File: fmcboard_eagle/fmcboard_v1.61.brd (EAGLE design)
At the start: 147 x 74 mm, 208 parts, among them IC1 OPA699ID, IC10 LM358, IC11 7805TV, IC12 SN74AUC2G66DCTR, IC13 SN74AUC2G66DCTR, IC14 SN74AUC2G66DCTR, IC15 SN74AUC2G66DCTR, IC16 DAC7578SPWR, IC17 SN74AUC2G66DCTR, IC18 SN74AUC2G66DCTR, IC19 SN74AUC2G66DCTR, IC2 DAC7578SPWR, IC20 SN74AUC2G66DCTR, IC21 74AUP2GU04GW, IC22 74AUP2GU04GW, IC23 74AUP2GU04GW, IC24 74AUP2GU04GW, IC25 LM358, IC26 AMS1117-1.8, IC3 LTC6229IMS8E#TRPBF, IC4 LTC6229IMS8E#TRPBF, IC5 LTC6229IMS8E#TRPBF, IC6 OPA699ID, IC7 OPA699ID, IC8 LM358, IC9 LM358, J1 8pin, J10 8pin, J11 8pin, J12 4p-2.54, J2 ASP-134604-01, J3 4p-2.54, J4 4p-2.54, J5 8pin, J6 4p-2.54, J7 4p-2.54, J8 4p-2.54, J9 8pin, U1 TXS0108EPWR, U2 STMICROELECTRONICS_L7905ACVST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

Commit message: routed 1.61
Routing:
- net GND: track 0.00 -> 449.9 mm, vias 0 -> 43
- net VS+: track 0.00 -> 330.0 mm, vias 0 -> 6
- net VS-: track 0.00 -> 305.3 mm, vias 0 -> 5
- net 1V8: track 0.00 -> 229.1 mm, vias 0 -> 10
- net SCLIN: track 0.00 -> 186.5 mm, vias 0 -> 2
- net SDAIN: track 0.00 -> 160.5 mm, vias 0 -> 4
- net H34: track 0.00 -> 156.1 mm, vias 0 -> 3
- net OPOUT1_H10: track 0.00 -> 151.4 mm, vias 0 -> 9
- net 1V8-: track 0.00 -> 144.2 mm, vias 0 -> 7
- net OPOUT2_H11: track 0.00 -> 140.5 mm, vias 0 -> 3
- net AR_SDAIN2: track 0.00 -> 136.9 mm, vias 0 -> 4
- net AR_SCLIN2: track 0.00 -> 133.5 mm, vias 0 -> 3
- net G37: track 0.00 -> 110.3 mm, vias 0 -> 2
- net G36: track 0.00 -> 109.7 mm, vias 0 -> 2
- net C10: track 0.00 -> 108.3 mm, vias 0 -> 4
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
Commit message: minor
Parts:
- moved C20 2.00 mm to (83.0, 9.00)
- moved R77 2.00 mm to (83.0, 11.0)
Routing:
- net GND: track 449.9 -> 451.6 mm
- net N$31: track 36.8 -> 35.9 mm, vias 2 -> 4
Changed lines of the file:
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@@
 <drawing>
 <settings>
-<setting alwaysvectorfont="no"/>
+<setting alwaysvectorfont="yes"/>
 <setting verticaltext="up"/>
 </settings>
@@
 <wire x1="38" y1="73" x2="38" y2="1" width="0.1524" layer="21"/>
 <text x="95.4" y="29.5" size="0.8128" layer="21">GNDs</text>
-<wire x1="39" y1="64" x2="139" y2="64" width="0.1524" layer="21"/>
+<wire x1="68" y1="64" x2="139" y2="64" width="0.1524" layer="21"/>
 <wire x1="127" y1="1" x2="127" y2="63" width="0.1524" layer="21"/>
-<wire x1="67" y1="63" x2="67" y2="1" width="0.1524" layer="21"/>
+<wire x1="67" y1="73" x2="67" y2="1" width="0.1524" layer="21"/>
 <wire x1="86" y1="63" x2="86" y2="1" width="0.1524" layer="21"/>
 <wire x1="109" y1="63" x2="109" y2="30" width="0.1524" layer="21"/>
@@
 <attribute name="SPICEPREFIX" value="R" x="71" y="9" size="1.778" layer="27" rot="R180" display="off"/>
 </element>
-<element name="R77" library="rcl" library_urn="urn:adsk.eagle:library:334" package="R0805" package3d_urn="urn:adsk.eagle:package:23553/2" value="100" x="83" y="9" smashed="yes">
-<attribute name="POPULARITY" value="85" x="83" y="9" size="1.778" layer="27" display="off"/>
-<attribute name="SPICEPREFIX" value="R" x="83" y="9" size="1.778" layer="27" display="off"/>
+<element name="R77" library="rcl" library_urn="urn:adsk.eagle:library:334" package="R0805" package3d_urn="urn:adsk.eagle:package:23553/2" value="100" x="83" y="11" smashed="yes">
+<attribute name="POPULARITY" value="85" x="83" y="11" size="1.778" layer="27" display="off"/>
+<attribute name="SPICEPREFIX" value="R" x="83" y="11" size="1.778" layer="27" display="off"/>
 </element>
 <element name="C17" library="SparkFun-Passives" package="0805" value="1uF" x="71" y="24" smashed="yes"/>
 <element name="C18" library="SparkFun-Passives" package="0805" value="1uF" x="83" y="22" smashed="yes" rot="R180"/>
 <element name="C19" library="SparkFun-Passives" package="0805" value="1uF" x="71" y="11" smashed="yes"/>
-<element name="C20" library="SparkFun-Passives" package="0805" value="1uF" x="83" y="11" smashed="yes" rot="R180"/>
+<element name="C20" library="SparkFun-Passives" package="0805" value="1uF" x="83" y="9" smashed="yes" rot="R180"/>
 <element name="J11" library="SparkFun-Connectors" library_urn="urn:adsk.eagle:library:513" package="1X08" package3d_urn="urn:adsk.eagle:package:38138/1" value="8pin" x="88.2" y="31.9" smashed="yes">
 <attribute name="PROD_ID" value="CONN-08438" x="88.2" y="31.9" size="1.778" layer="27" display="off"/>
@@
 <wire x1="64" y1="30.125" x2="64" y2="29" width="0.3048" layer="1"/>
 <wire x1="64" y1="29" x2="63.9" y2="29" width="0.3048" layer="1"/>
-<wire x1="83.875" y1="12.125" x2="83.875" y2="11" width="0.3048" layer="1"/>
-<wire x1="83.875" y1="11" x2="83.9" y2="11" width="0.3048" layer="1"/>
+<wire x1="82.875" y1="7.125" x2="82.875" y2="9" width="0.3048" layer="1"/>
+<wire x1="82.875" y1="9" x2="83.9" y2="9" width="0.3048" layer="1"/>
 <wire x1="78.125" y1="21.125" x2="78.125" y2="20" width="0.3048" layer="1"/>
 <wire x1="78.125" y1="20" x2="78.1" y2="20" width="0.3048" layer="1"/>
@@
 <wire x1="114.25" y1="23" x2="113" y2="23" width="0.3048" layer="1"/>
 <wire x1="113" y1="23" x2="112.938" y2="22.975" width="0.3048" layer="1"/>
-<wire x1="57.125" y1="8.25" x2="57.125" y2="7" width="0.3048" layer="1"/>
-<wire x1="57.125" y1="7" x2="57.05" y2="7" width="0.3048" layer="1"/>
 <wire x1="57.125" y1="8.25" x2="57.279396875" y2="8.25" width="0.3048" layer="2"/>
 <wire x1="88.125" y1="24.25" x2="88.125" y2="23" width="0.3048" layer="1"/>
@@
 <via x="55.875" y="33.125" extent="1-16" drill="0.3048"/>
 <via x="64" y="30.125" extent="1-16" drill="0.3048"/>
-<via x="83.875" y="12.125" extent="1-16" drill="0.3048"/>
+<via x="82.875" y="7.125" extent="1-16" drill="0.3048"/>
 <via x="78.125" y="21.125" extent="1-16" drill="0.3048"/>
 <via x="56.125" y="47" extent="1-16" drill="0.3048"/>
@@
 <wire x1="13.175" y1="45.255" x2="22.205" y2="45.255" width="0.3048" layer="16"/>
 <wire x1="22.205" y1="45.255" x2="23" y2="46.05" width="0.3048" layer="16"/>
+<wire x1="57.125" y1="8.25" x2="57.125" y2="7.075" width="0.3048" layer="1"/>
+<wire x1="57.125" y1="7.075" x2="57.05" y2="7" width="0.3048" layer="1"/>
 </signal>
 <signal name="IO1">
@@
 <wire x1="80.625" y1="8.25" x2="79" y2="8.25" width="0.3048" layer="15"/>
 <wire x1="81.25" y1="8.25" x2="80.625" y2="8.25" width="0.3048" layer="1"/>
-<wire x1="82" y1="9" x2="81.25" y2="8.25" width="0.3048" layer="1"/>
+<wire x1="82.05" y1="9.05" x2="81.25" y2="8.25" width="0.3048" layer="1"/>
 <wire x1="79" y1="9" x2="78.95" y2="9.025" width="0.3048" layer="1"/>
-<wire x1="82" y1="9" x2="82.05" y2="9" width="0.3048" layer="1"/>
-<wire x1="82.125" y1="9.125" x2="82.125" y2="11" width="0.3048" layer="1"/>
-<wire x1="82.125" y1="11" x2="82.1" y2="11" width="0.3048" layer="1"/>
-<wire x1="82.125" y1="9.125" x2="82.05" y2="9" width="0.3048" layer="1"/>
 <via x="79" y="8.25" extent="1-16" drill="0.3048"/>
 <via x="80.625" y="8.25" extent="1-16" drill="0.3048"/>
+<wire x1="82.1" y1="9" x2="82.05" y2="9.05" width="0.3048" layer="1"/>
+<wire x1="82.05" y1="9.05" x2="82.05" y2="11" width="0.3048" layer="1"/>
 </signal>
 <signal name="N$16">
@@
 <wire x1="54.875" y1="19.75" x2="54.8" y2="19.635" width="0.3048" layer="1"/>
 <wire x1="57" y1="21" x2="57.05" y2="21" width="0.3048" layer="1"/>
-<wire x1="83.875" y1="9.25" x2="83.875" y2="9" width="0.3048" layer="1"/>
-<wire x1="83" y1="10.125" x2="83.875" y2="9.25" width="0.3048" layer="1"/>
-<wire x1="79" y1="10.125" x2="83" y2="10.125" width="0.3048" layer="15"/>
-<wire x1="70.75" y1="18.375" x2="79" y2="10.125" width="0.3048" layer="15"/>
 <wire x1="70.25" y1="18.375" x2="70.75" y2="18.375" width="0.3048" layer="1"/>
 <wire x1="65.25" y1="23.375" x2="70.25" y2="18.375" width="0.3048" layer="1"/>
 <wire x1="59.375" y1="23.375" x2="65.25" y2="23.375" width="0.3048" layer="1"/>
 <wire x1="57.125" y1="21.125" x2="59.375" y2="23.375" width="0.3048" layer="1"/>
-<wire x1="83.875" y1="9" x2="83.95" y2="9" width="0.3048" layer="1"/>
 <wire x1="57.125" y1="21.125" x2="57.05" y2="21" width="0.3048" layer="1"/>
-<via x="83" y="10.125" extent="1-16" drill="0.3048"/>
 <via x="70.75" y="18.375" extent="1-16" drill="0.3048"/>
+<wire x1="83.95" y1="11" x2="81.95" y2="13" width="0.3048" layer="1"/>
+<wire x1="81.95" y1="13" x2="81" y2="13" width="0.3048" layer="1"/>
+<via x="81" y="13" extent="1-16" drill="0.35"/>
+<wire x1="81" y1="13" x2="79" y2="13" width="0.3048" layer="15"/>
+<via x="79" y="13" extent="1-16" drill="0.35"/>
+<wire x1="79" y1="13" x2="76" y2="13" width="0.3048" layer="1"/>
+<wire x1="76" y1="13" x2="75" y2="14" width="0.3048" layer="1"/>
+<via x="75" y="14" extent="1-16" drill="0.35"/>
+<wire x1="75" y1="14" x2="70.75" y2="18.25" width="0.3048" layer="15"/>
+<wire x1="70.75" y1="18.25" x2="70.75" y2="18.375" width="0.3048" layer="15"/>
 </signal>
 <signal name="N$32">

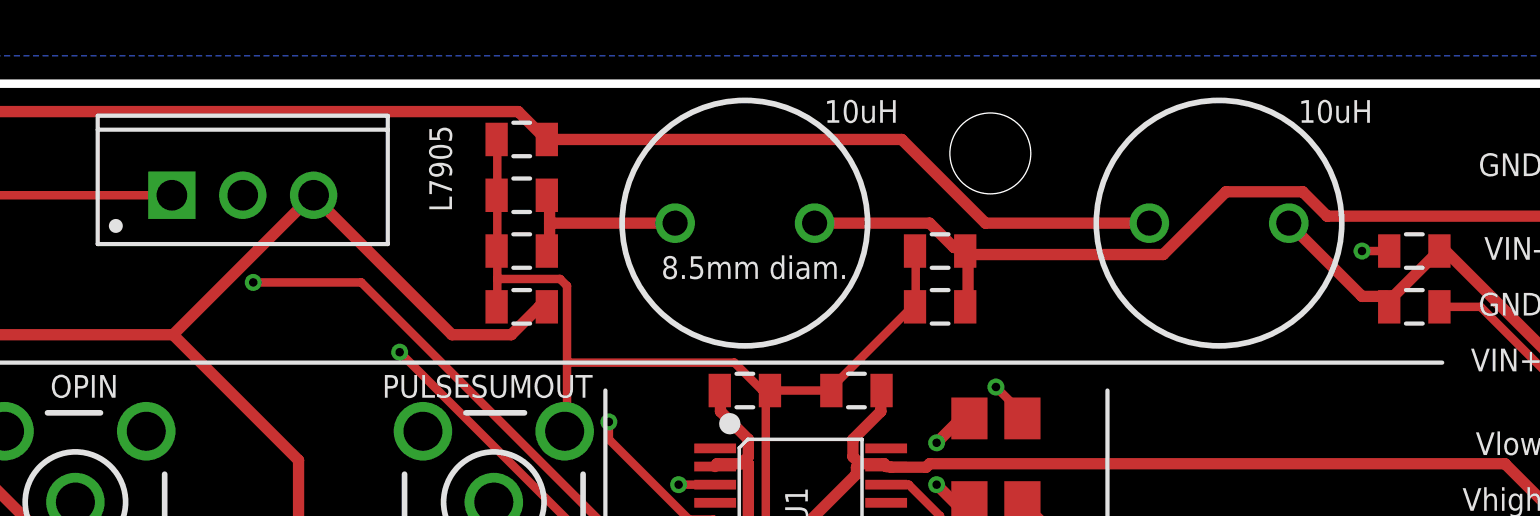
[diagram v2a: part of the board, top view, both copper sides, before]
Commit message: smd inductors
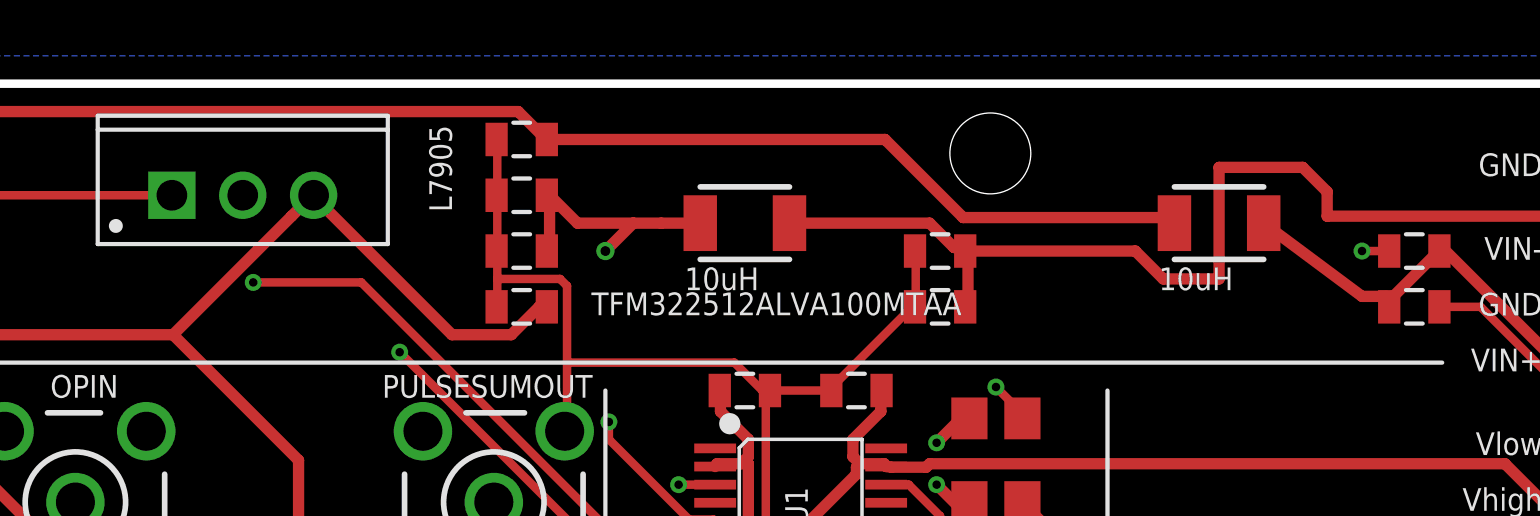
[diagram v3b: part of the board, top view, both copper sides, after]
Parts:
- L1, L2: device rcl:6000-XXXX-RC -> SparkFun-Passives:1210
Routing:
- net VIN-: track 32.4 -> 37.7 mm
- net VIN+CLEAN: track 65.0 -> 65.9 mm
- net VIN+: track 15.6 -> 16.3 mm
- net VIN-CLEAN: track 22.8 -> 23.3 mm, vias 0 -> 1
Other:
- board text removed: "8.5mm diam."
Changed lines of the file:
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@@
 <drawing>
 <settings>
-<setting alwaysvectorfont="yes"/>
+<setting alwaysvectorfont="no"/>
 <setting verticaltext="up"/>
 </settings>
@@
 <text x="27.6" y="66.5" size="0.8128" layer="21" rot="R180">VS+</text>
 <text x="24.6" y="66.5" size="0.8128" layer="21" rot="R180">VS-</text>
-<text x="111" y="67" size="0.8128" layer="21">8.5mm diam.</text>
 <text x="103.5" y="69.4" size="0.8128" layer="21" rot="R90">L7905</text>
 <text x="39.3" y="48.5" size="0.8128" layer="21">DACP1 P2 P3 P4  DACN1 N2 N3 N4</text>
@@
 <attribute name="VALUE" x="81.62" y="68.92" size="0.8128" layer="21" ratio="10" rot="R90"/>
 </element>
-<element name="L1" library="rcl" library_urn="urn:adsk.eagle:library:334" package="6000-XXXX-RC" package3d_urn="urn:adsk.eagle:package:23538/1" value="10uH" x="131" y="69" smashed="yes" rot="R180">
-<attribute name="POPULARITY" value="5" x="131" y="69" size="0.8128" layer="27" rot="R180" display="off"/>
-<attribute name="SPICEPREFIX" value="L" x="131" y="69" size="0.8128" layer="27" rot="R180" display="off"/>
-<attribute name="VALUE" x="136.5056" y="73.4106" size="0.8128" layer="21" rot="R180"/>
-</element>
-<element name="L2" library="rcl" library_urn="urn:adsk.eagle:library:334" package="6000-XXXX-RC" package3d_urn="urn:adsk.eagle:package:23538/1" value="10uH" x="114" y="69" smashed="yes" rot="R180">
-<attribute name="POPULARITY" value="5" x="114" y="69" size="0.8128" layer="27" rot="R180" display="off"/>
-<attribute name="SPICEPREFIX" value="L" x="114" y="69" size="0.8128" layer="27" rot="R180" display="off"/>
-<attribute name="VALUE" x="119.5056" y="73.4106" size="0.8128" layer="21" rot="R180"/>
+<element name="L1" library="SparkFun-Passives" package="1210" value="10uH" x="131" y="69" smashed="yes" rot="R180">
+<attribute name="LCSC" value="C1882517" x="131" y="69" size="1.778" layer="27" rot="R180" display="off"/>
+<attribute name="MPN" value="TFM322512ALVA100MTAA" x="131" y="69" size="1.778" layer="27" rot="R180" display="off"/>
+<attribute name="VALUE" x="131.5056" y="67.4106" size="0.8128" layer="21" rot="R180"/>
+</element>
+<element name="L2" library="SparkFun-Passives" package="1210" value="10uH" x="114" y="69" smashed="yes" rot="R180">
+<attribute name="LCSC" value="C1882517" x="114" y="69" size="1.778" layer="27" rot="R180" display="off"/>
+<attribute name="MPN" value="TFM322512ALVA100MTAA" x="108.5" y="65.7" size="0.8128" layer="21"/>
+<attribute name="VALUE" x="114.5056" y="67.4106" size="0.8128" layer="21" rot="R180"/>
 </element>
 <element name="C42" library="SparkFun-Passives" package="0805" value="0.1uF" x="138" y="68" smashed="yes" rot="R180"/>
@@
 <wire x1="84.375" y1="65" x2="83.375" y2="66" width="0.4064" layer="1"/>
 <wire x1="93.5" y1="65" x2="84.375" y2="65" width="0.4064" layer="1"/>
-<wire x1="98.5" y1="70" x2="93.5" y2="65" width="0.4064" layer="1"/>
+<wire x1="98.5" y1="70" x2="97.75" y2="69.25" width="0.4064" layer="1"/>
+<wire x1="97.75" y1="69.25" x2="93.5" y2="65" width="0.4064" layer="1"/>
 <wire x1="98.5" y1="70" x2="98.54" y2="70" width="0.4064" layer="1"/>
 <wire x1="106.625" y1="66" x2="106.9" y2="66" width="0.4064" layer="1"/>
@@
 <wire x1="71.46" y1="70.46" x2="74" y2="73" width="0.4064" layer="1"/>
 <wire x1="83.125" y1="68" x2="83.1" y2="68" width="0.4064" layer="1"/>
-<wire x1="119.625" y1="72" x2="106.9" y2="72" width="0.4064" layer="1"/>
-<wire x1="122.625" y1="69" x2="119.625" y2="72" width="0.4064" layer="1"/>
-<wire x1="128.5" y1="69" x2="122.625" y2="69" width="0.4064" layer="1"/>
+<wire x1="119.025" y1="72" x2="106.9" y2="72" width="0.4064" layer="1"/>
+<wire x1="121.825" y1="69.2" x2="119.025" y2="72" width="0.4064" layer="1"/>
+<wire x1="129.4" y1="69" x2="129.2" y2="69.2" width="0.4064" layer="1"/>
+<wire x1="129.2" y1="69.2" x2="121.825" y2="69.2" width="0.4064" layer="1"/>
 <wire x1="84.25" y1="72.875" x2="84" y2="72.875" width="0.4064" layer="1"/>
 <wire x1="84.375" y1="73" x2="84.25" y2="72.875" width="0.4064" layer="1"/>
@@
 <contactref element="U2" pad="2"/>
 <contactref element="C40" pad="2"/>
-<wire x1="107" y1="70" x2="107" y2="69" width="0.4064" layer="1"/>
-<wire x1="107" y1="69" x2="107" y2="68" width="0.4064" layer="1"/>
+<wire x1="107" y1="70" x2="107" y2="68" width="0.4064" layer="1"/>
 <wire x1="107" y1="68" x2="106.9" y2="68" width="0.4064" layer="1"/>
 <wire x1="107" y1="70" x2="106.9" y2="70" width="0.4064" layer="1"/>
-<wire x1="111.5" y1="69" x2="107" y2="69" width="0.4064" layer="1"/>
-<wire x1="96.75" y1="70" x2="96" y2="70" width="0.4064" layer="15"/>
-<wire x1="98" y1="68.75" x2="96.75" y2="70" width="0.4064" layer="15"/>
-<wire x1="111.25" y1="68.75" x2="98" y2="68.75" width="0.4064" layer="15"/>
-<wire x1="111.5" y1="69" x2="111.25" y2="68.75" width="0.4064" layer="15"/>
+<wire x1="96" y1="70" x2="96.75" y2="70" width="0.4064" layer="15"/>
+<wire x1="112.4" y1="69" x2="111" y2="69" width="0.4064" layer="1"/>
+<wire x1="110" y1="69" x2="108" y2="69" width="0.4064" layer="1"/>
+<wire x1="108" y1="69" x2="107" y2="70" width="0.4064" layer="1"/>
+<wire x1="98.75" y1="68" x2="109" y2="68" width="0.4064" layer="15"/>
+<via x="109" y="68" extent="1-16" drill="0.35"/>
+<wire x1="109" y1="68" x2="110" y2="69" width="0.4064" layer="1"/>
+<wire x1="110" y1="69" x2="111" y2="69" width="0.4064" layer="1"/>
+<wire x1="96.75" y1="70" x2="98.75" y2="68" width="0.4064" layer="15"/>
 </signal>
 <signal name="VIN+" class="1">
@@
 <wire x1="138.875" y1="68" x2="138.9" y2="68" width="0.4064" layer="1"/>
 <wire x1="136.125" y1="66.375" x2="137" y2="66.375" width="0.4064" layer="1"/>
-<wire x1="133.5" y1="69" x2="136.125" y2="66.375" width="0.4064" layer="1"/>
+<wire x1="132.6" y1="69" x2="136.125" y2="66.375" width="0.4064" layer="1"/>
 <wire x1="137" y1="66.375" x2="137.1" y2="66" width="0.4064" layer="1"/>
 <wire x1="142.875" y1="64.25" x2="145" y2="64.25" width="0.4064" layer="1"/>
@@
 <wire x1="121.5" y1="68.125" x2="121.75" y2="68.125" width="0.4064" layer="1"/>
 <wire x1="120.625" y1="69" x2="121.5" y2="68.125" width="0.4064" layer="1"/>
-<wire x1="116.5" y1="69" x2="120.625" y2="69" width="0.4064" layer="1"/>
+<wire x1="115.6" y1="69" x2="120.625" y2="69" width="0.4064" layer="1"/>
 <wire x1="121.75" y1="68.125" x2="121.9" y2="68" width="0.4064" layer="1"/>
 <wire x1="134.875" y1="69.25" x2="145" y2="69.25" width="0.4064" layer="1"/>
-<wire x1="134" y1="70.125" x2="134.875" y2="69.25" width="0.4064" layer="1"/>
-<wire x1="131.25" y1="70.125" x2="134" y2="70.125" width="0.4064" layer="1"/>
-<wire x1="129" y1="67.875" x2="131.25" y2="70.125" width="0.4064" layer="1"/>
-<wire x1="122.125" y1="67.875" x2="129" y2="67.875" width="0.4064" layer="1"/>
 <wire x1="145" y1="69.25" x2="145" y2="69.24" width="0.4064" layer="1"/>
-<wire x1="122.125" y1="67.875" x2="121.9" y2="68" width="0.4064" layer="1"/>
+<wire x1="121.9" y1="68" x2="128" y2="68" width="0.4064" layer="1"/>
+<wire x1="128" y1="68" x2="129" y2="67" width="0.4064" layer="1"/>
+<wire x1="129" y1="67" x2="131" y2="67" width="0.4064" layer="1"/>
+<wire x1="131" y1="67" x2="131" y2="71" width="0.4064" layer="1"/>
+<wire x1="131" y1="71" x2="134" y2="71" width="0.4064" layer="1"/>
+<wire x1="134" y1="71" x2="134.875" y2="70.125" width="0.4064" layer="1"/>
+<wire x1="134.875" y1="70.125" x2="134.875" y2="69.25" width="0.4064" layer="1"/>
 </signal>
 <signal name="DACP2">
